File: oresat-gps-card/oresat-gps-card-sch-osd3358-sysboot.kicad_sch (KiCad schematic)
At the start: 28 parts, among them J5 Conn_01x06, U1 OSD3358-512M-BSM

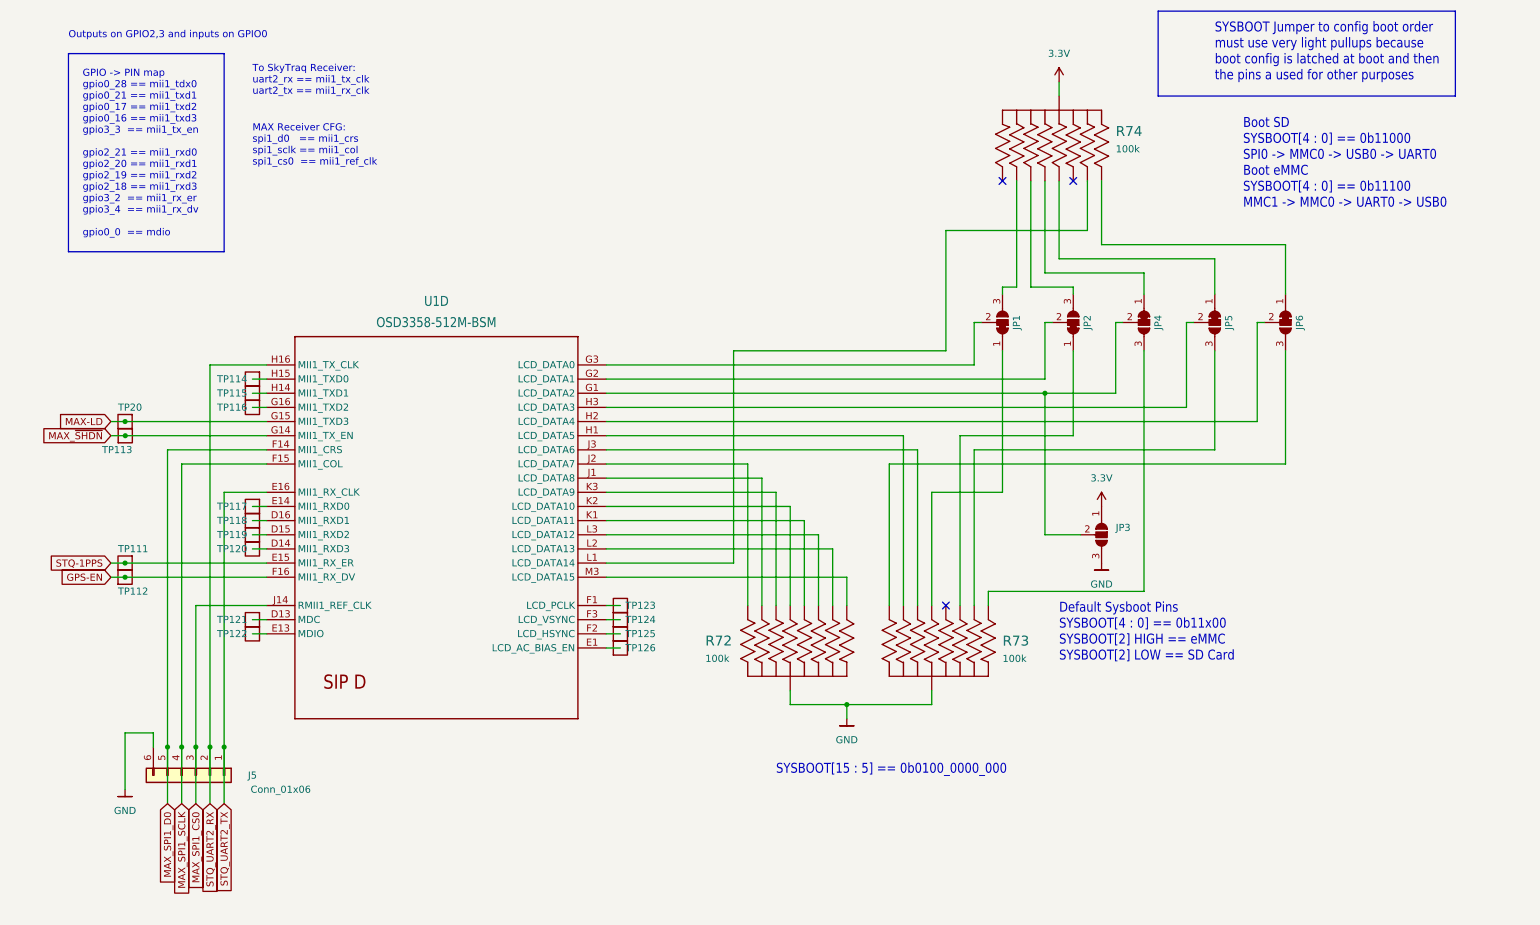
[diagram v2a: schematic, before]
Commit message: Updated GPS card with changes from C3 and notes. Fixed library issues
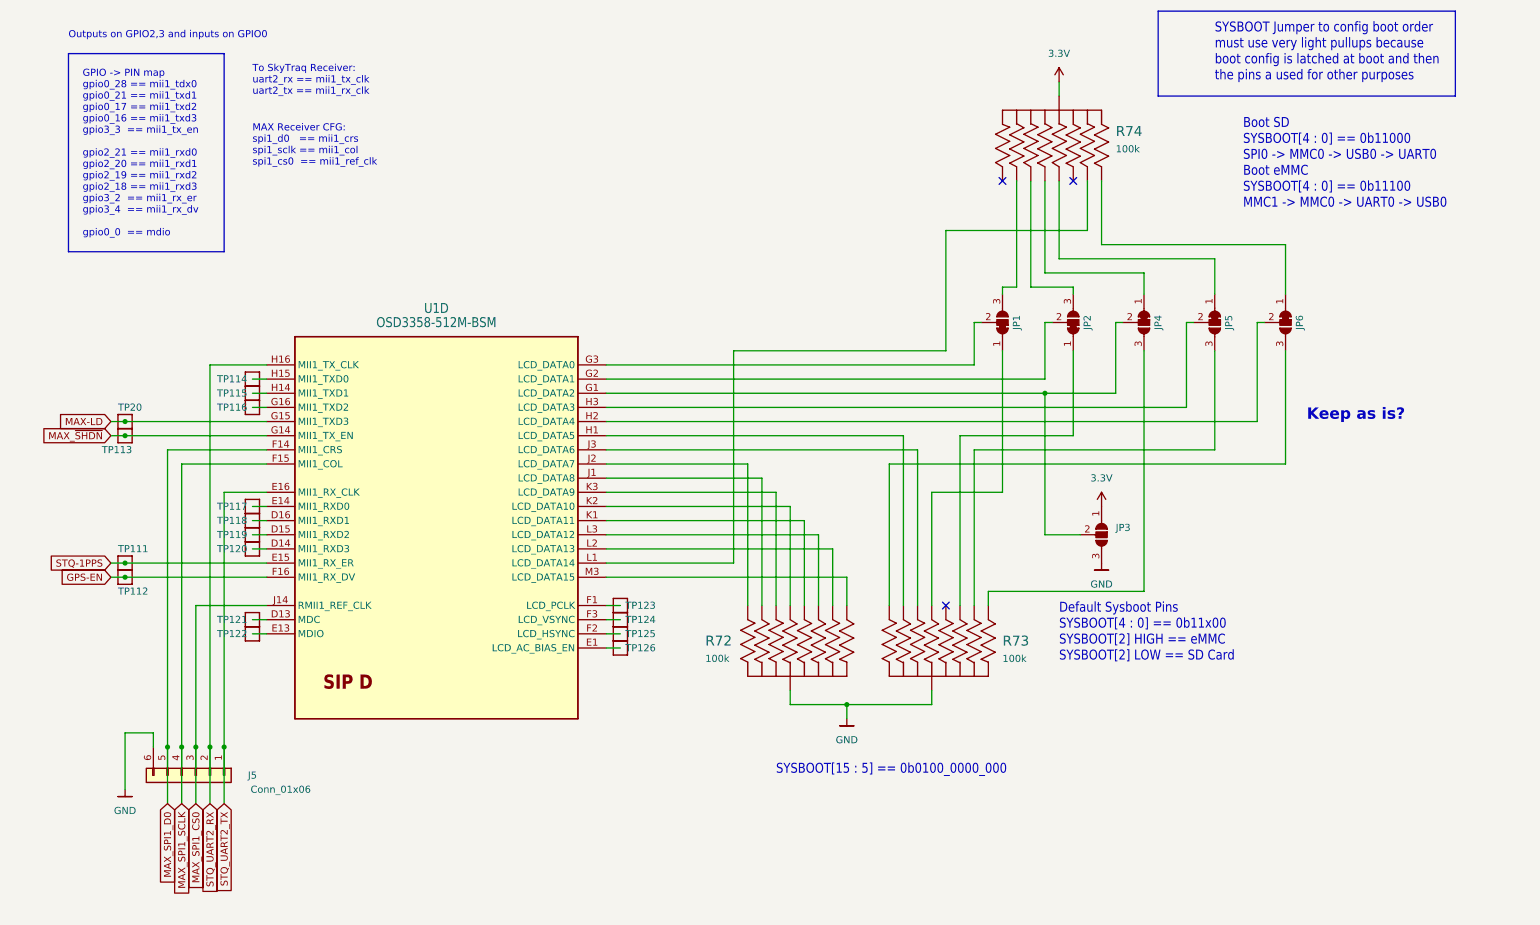
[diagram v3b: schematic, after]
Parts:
- R72, R73, R74: footprint oresat-footprints:R-ARRAY_EXBA-M -> oresat-passives:Panasonic_Resistor_Array_EXBA10; symbol R-EXB-A10P391j:EXB-A10P391J -> oresat-passives:EXB-A10P391J
- TP111, TP112, TP113, TP114, TP115, TP116, TP117, TP118, TP119, TP120, TP121, TP122, TP123, TP124, TP125, TP126, TP20: value Test-Point -> 0.03x0.04; footprint OreSat-TestPoint:PAD.03X.04 -> oresat-misc:TestPoint_Pad_D1.0mm; symbol OreSat-TestPoint:Test-Point -> oresat-misc:Test-Point-1mm-round
- U1: footprint oresat-footprints:U-Octavo-OSD335X-BGA-256 -> oresat-ics:U-Octavo-OSD335X-BGA-256; symbol U-OSD3358-512M-BSM:OSD3358-512M-BSM -> oresat-ics:OSD3358-512M-BSM
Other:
- note added: "Keep as is?"

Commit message: Updated GPS card
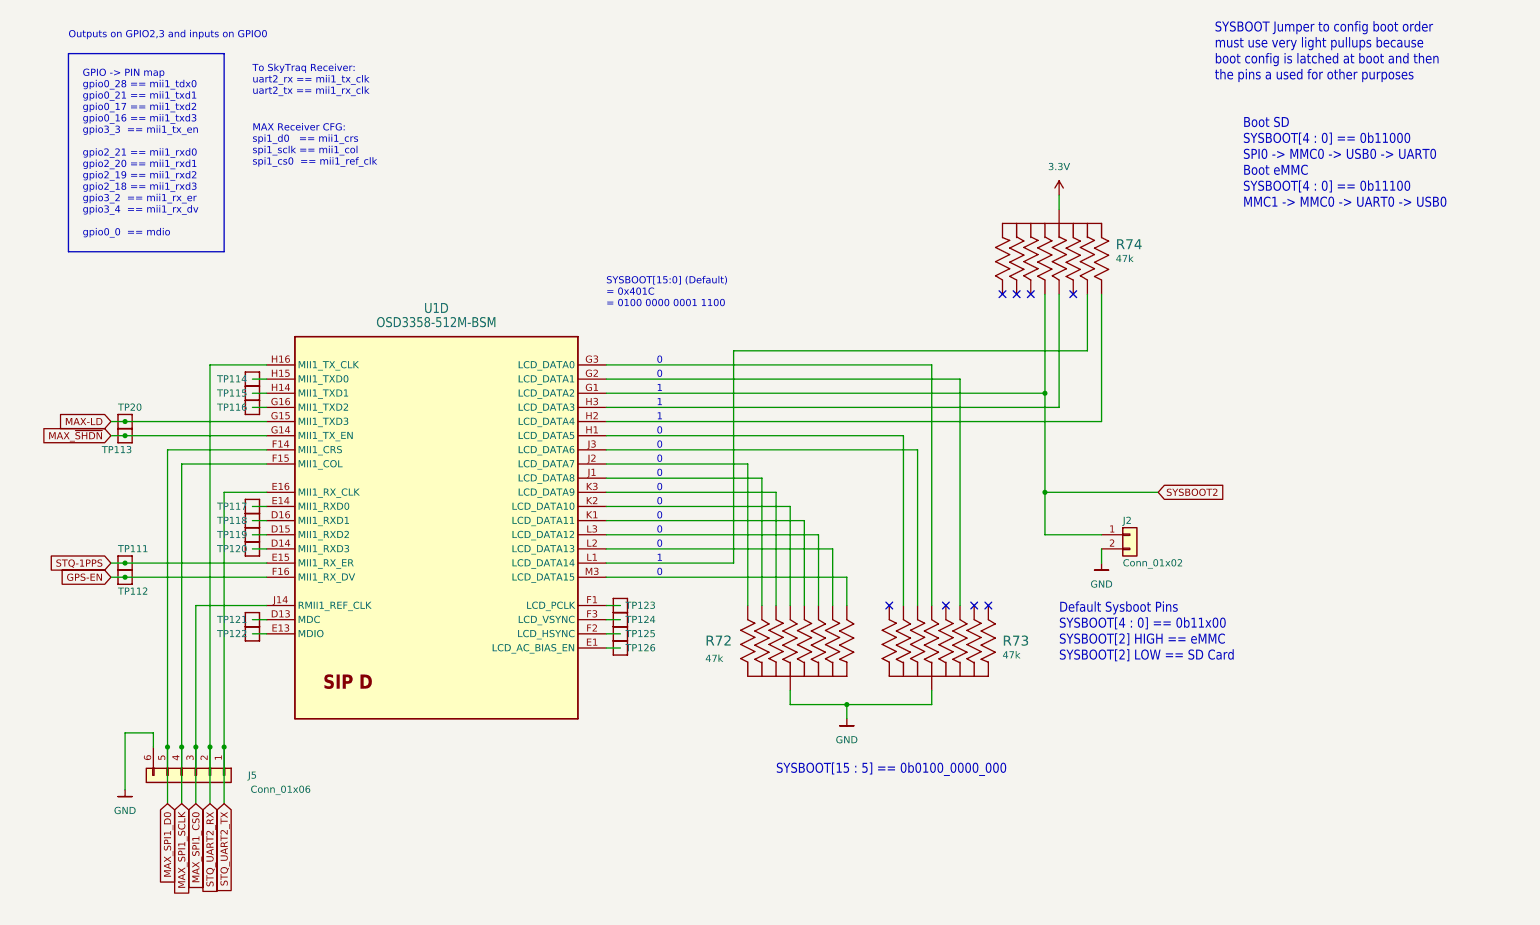
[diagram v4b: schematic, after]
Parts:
- removed JP1, JP2, JP4, JP5, JP6: SolderJumper_3_Bridged12, oresat-footprints:SMT-JUMPER_3_1-NC_TRACE_SILK, symbol Jumper:SolderJumper_3_Bridged12
- removed JP3: SolderJumper_3_Open, Connector_PinHeader_2.54mm:PinHeader_1x03_P2.54mm_Vertical, symbol Jumper:SolderJumper_3_Open
- added J2: Conn_01x02, Connector_PinHeader_2.54mm:PinHeader_1x02_P2.54mm_Vertical, symbol Connector_Generic:Conn_01x02
- R72, R73, R74: value 100k -> 47k
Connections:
- net GND: now also J2.2 (Pin_2)
- net at R73.2 (22): now also U1.G2 (LCD_DATA1)
- net at R73.3 (33): now also U1.G3 (LCD_DATA0)
- net SYSBOOT2: now reaches U1.G1 (LCD_DATA2)
- net SYSBOOT2: now also R74.8 (88), J2.1 (Pin_1)
- net at U1.H2 (LCD_DATA4): now also R74.6 (66)
- net at U1.H3 (LCD_DATA3): now also R74.3 (33)
- no-connect marks 3 -> 8
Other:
- note added: "0"
- note added: "1"
- note added: "SYSBOOT[15:0] (Default) = 0x401C = 0100 0000 0001 1100"
- note removed: "Keep as is?"
- moved on the sheet: R74

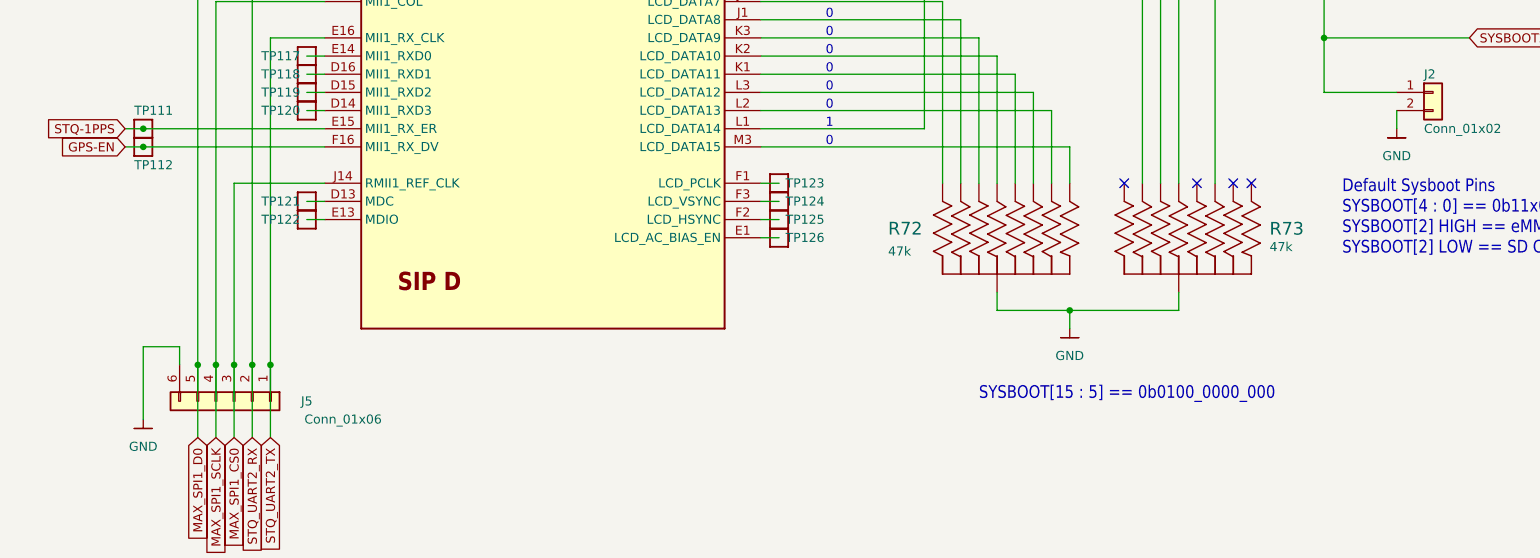
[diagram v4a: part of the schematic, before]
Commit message: Cleaned up ERC and DRC errors on GPS card
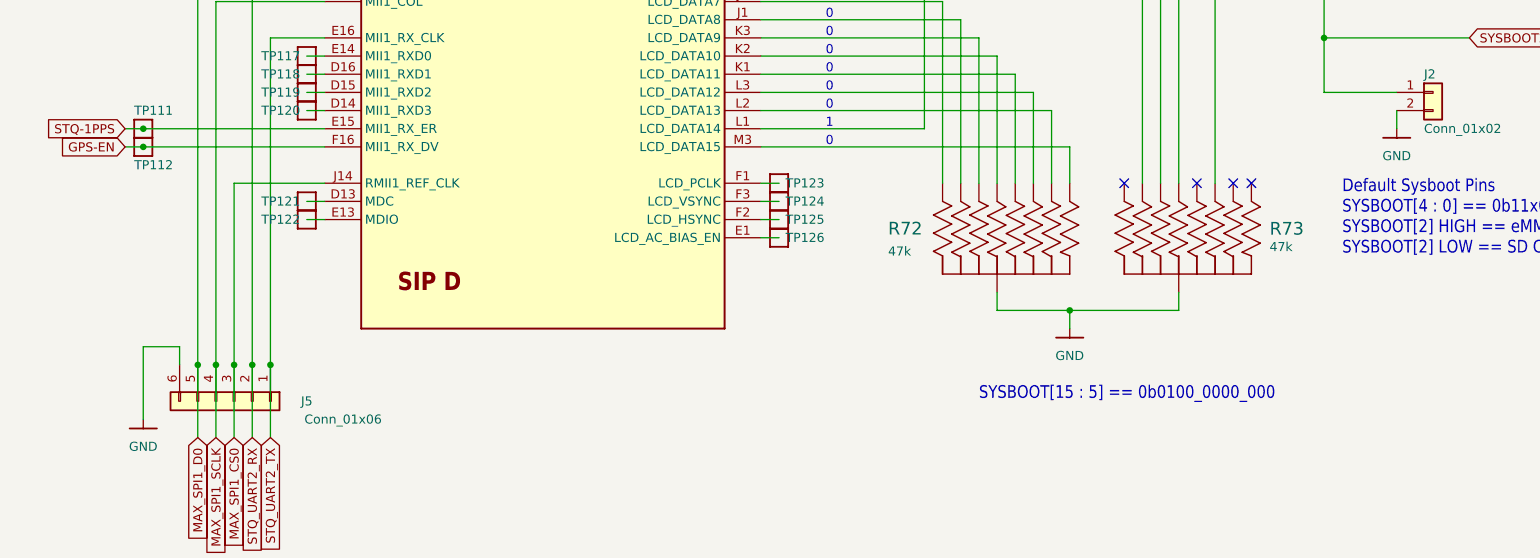
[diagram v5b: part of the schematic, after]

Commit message: Updated KiCAD 8, updated schematic sheet info, polished some schematic things, and made DNP parts DNP.
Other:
- title: (none) -> OreSat GPS Card

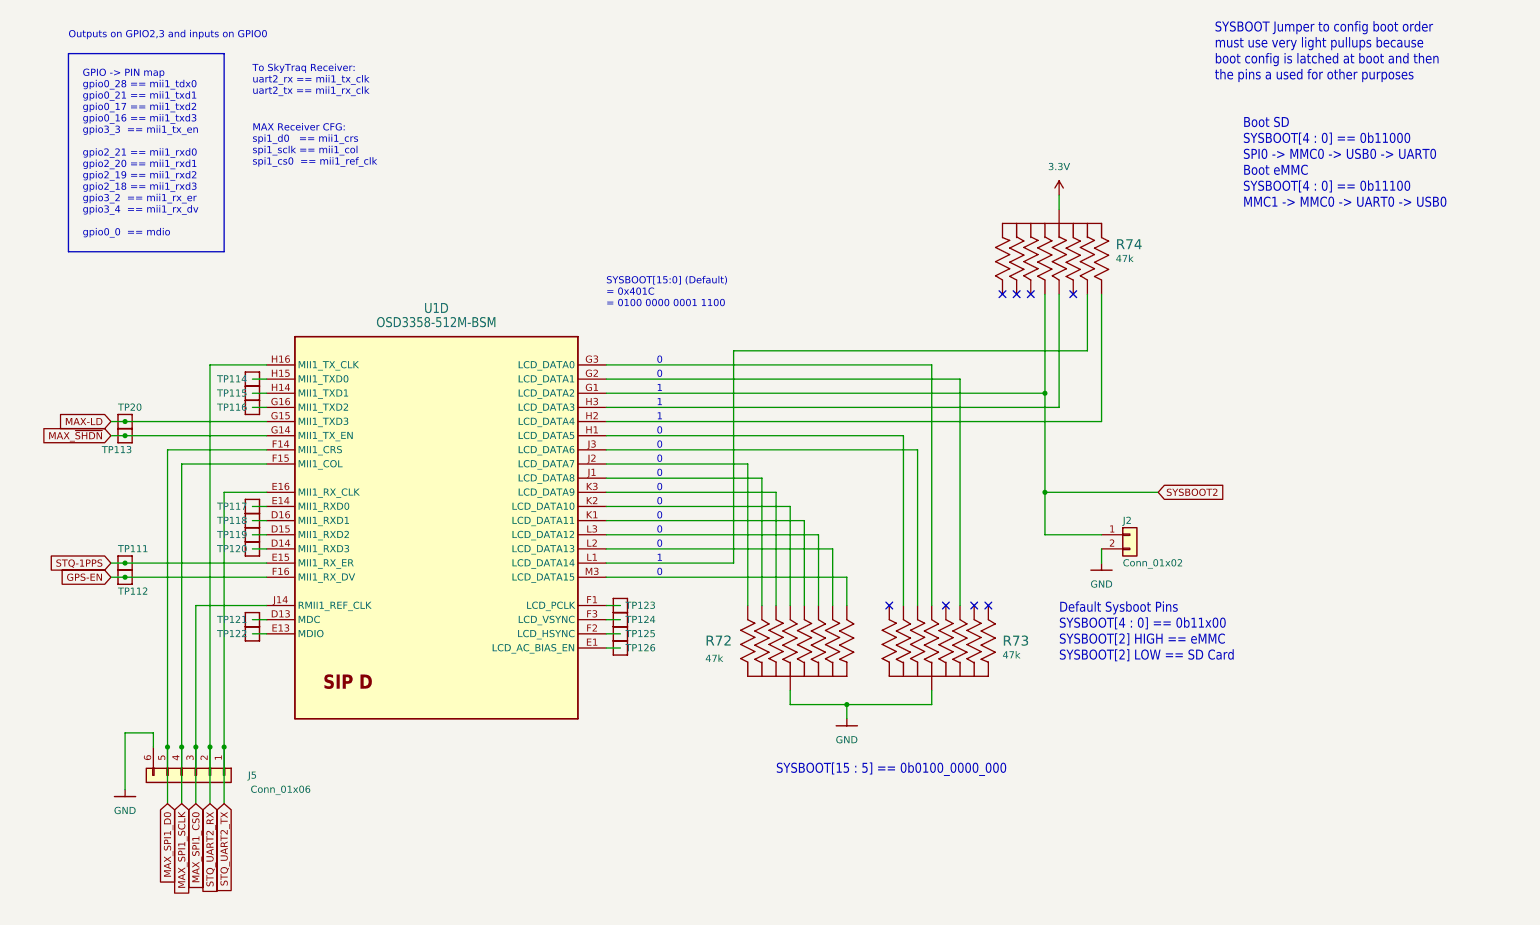
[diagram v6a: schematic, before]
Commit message: updated symbols and started new 2771 symbol
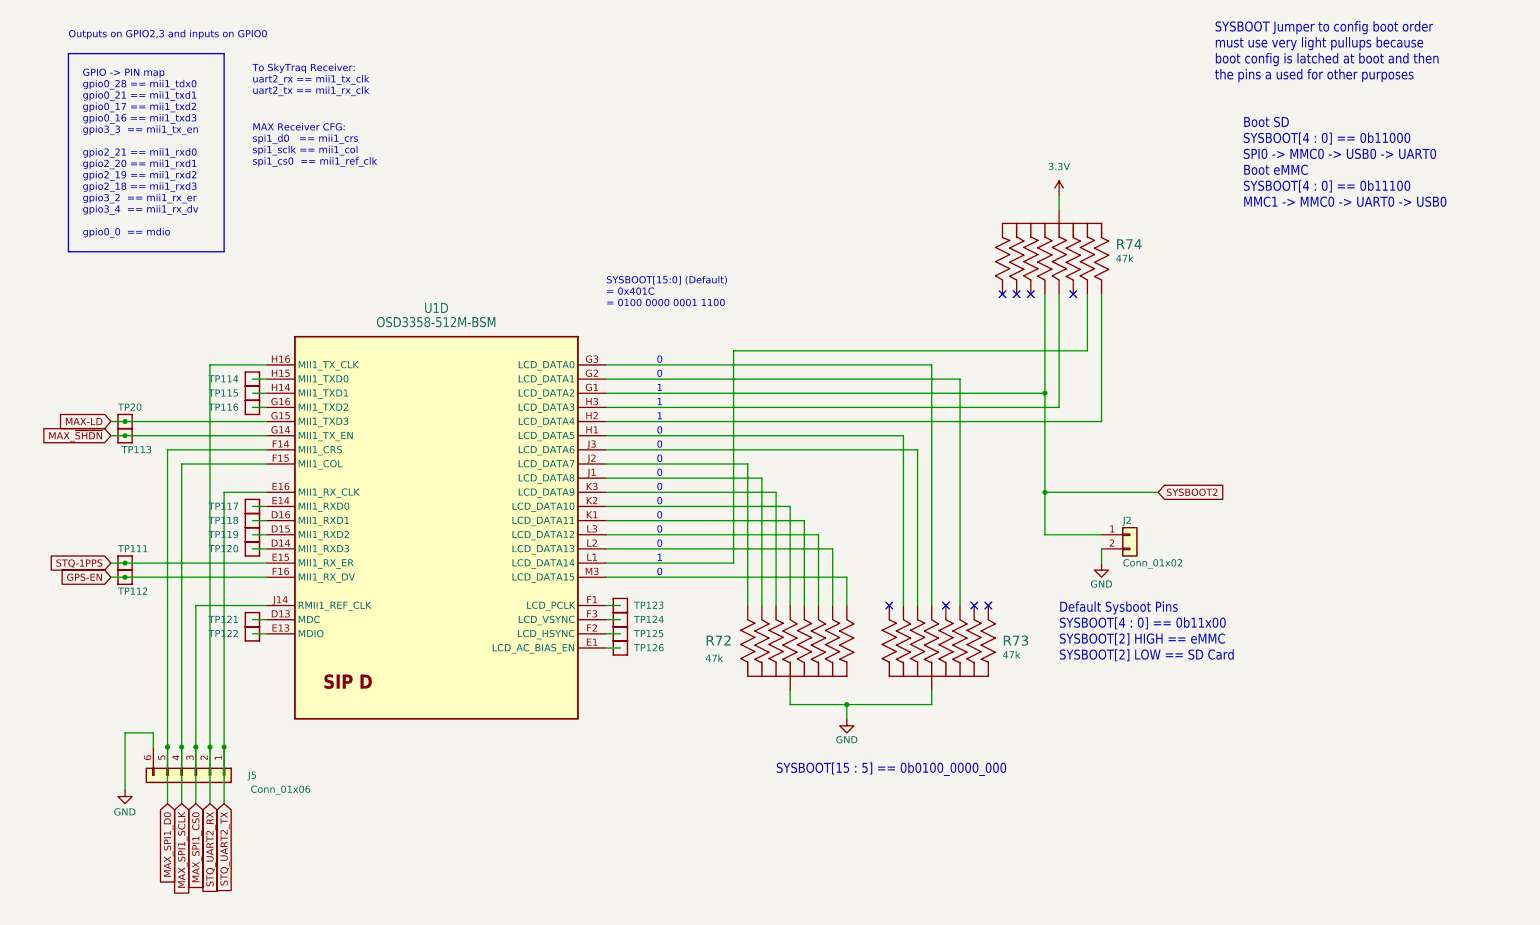
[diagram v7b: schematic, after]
